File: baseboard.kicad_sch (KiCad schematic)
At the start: 27 parts, among them J10 AS7265X, J11 Conn_02x20_Odd_Even, J12 TFTLCD, J5 Screw_Terminal_01x02, J6 DCMI_CAMERA, J7 LCD_CHAR, J8 Conn_01x03, J9 Conn_01x03, U2 LM2676S-5, U3 AMS1117-3.3

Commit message: snapshot
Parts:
- removed J12: TFTLCD, Connector_PinHeader_2.54mm:PinHeader_1x09_P2.54mm_Vertical, symbol Connector_Generic:Conn_01x09
- added H1, H2, H3, H4: MountingHole, MountingHole:MountingHole_3.2mm_M3, symbol Mechanical:MountingHole
- added J13: UserGPIO, Connector_PinHeader_2.54mm:PinHeader_2x05_P2.54mm_Vertical, symbol Connector_Generic:Conn_02x05_Odd_Even
- added J14: TFT_LCD, Connector_PinHeader_2.54mm:PinHeader_1x14_P2.54mm_Vertical, symbol Connector_Generic:Conn_01x14
- J11: value Conn_02x20_Odd_Even -> TFT_LCD2
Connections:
- net GND: now also J13.1 (Pin_1), J13.10 (Pin_10), J13.3 (Pin_3), J13.5 (Pin_5), J13.7 (Pin_7), J13.9 (Pin_9), J14.2 (Pin_2)
- net PB0: now also J11.39 (Pin_39), J14.8 (Pin_8)
- net PB1: now also J14.5 (Pin_5)
- net PB12: now also J14.3 (Pin_3)
- net PB13: now also J14.7 (Pin_7)
- net PB14: now also J14.9 (Pin_9)
- net PB15: now also J14.6 (Pin_6)
- net PB8: now also J11.34 (Pin_34)
- net PB9: now also J11.35 (Pin_35)
- net PC4: now also J14.4 (Pin_4)
- net VCC: now also J14.1 (Pin_1)
- net PC5: now reaches J11.36 (Pin_36)
- net PC5: now also J14.14 (Pin_14)
- net TE renamed PD2
- new net PA0: J13.8 (Pin_8)
- new net PA15: J14.11 (Pin_11)
- new net PA5: J14.10 (Pin_10)
- new net PB4: J14.13 (Pin_13)
- new net PB5: J14.12 (Pin_12)
- new net PC0: J13.2 (Pin_2)
- new net PC2: J13.4 (Pin_4)
- new net PC3: J13.6 (Pin_6)
- no-connect marks 0 -> 14
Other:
- moved on the sheet: C11, C12, C13, C14, C15, C16, C17, D2, D3, D4, J11, J5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

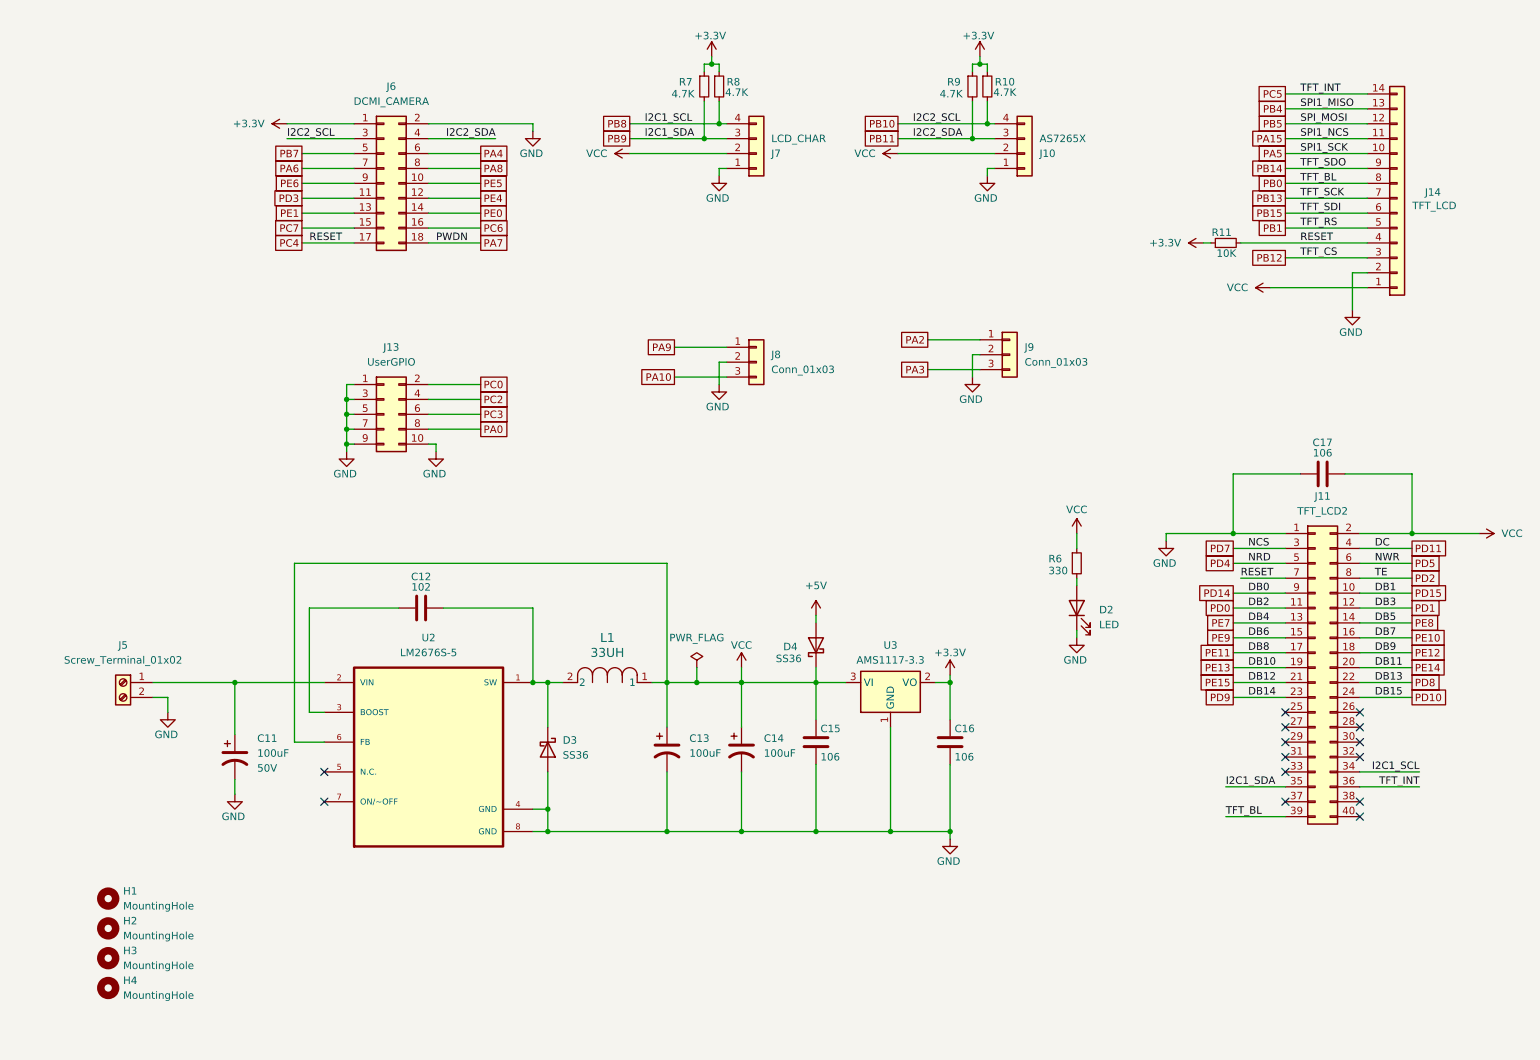
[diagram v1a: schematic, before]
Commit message: add servos and fan outputs
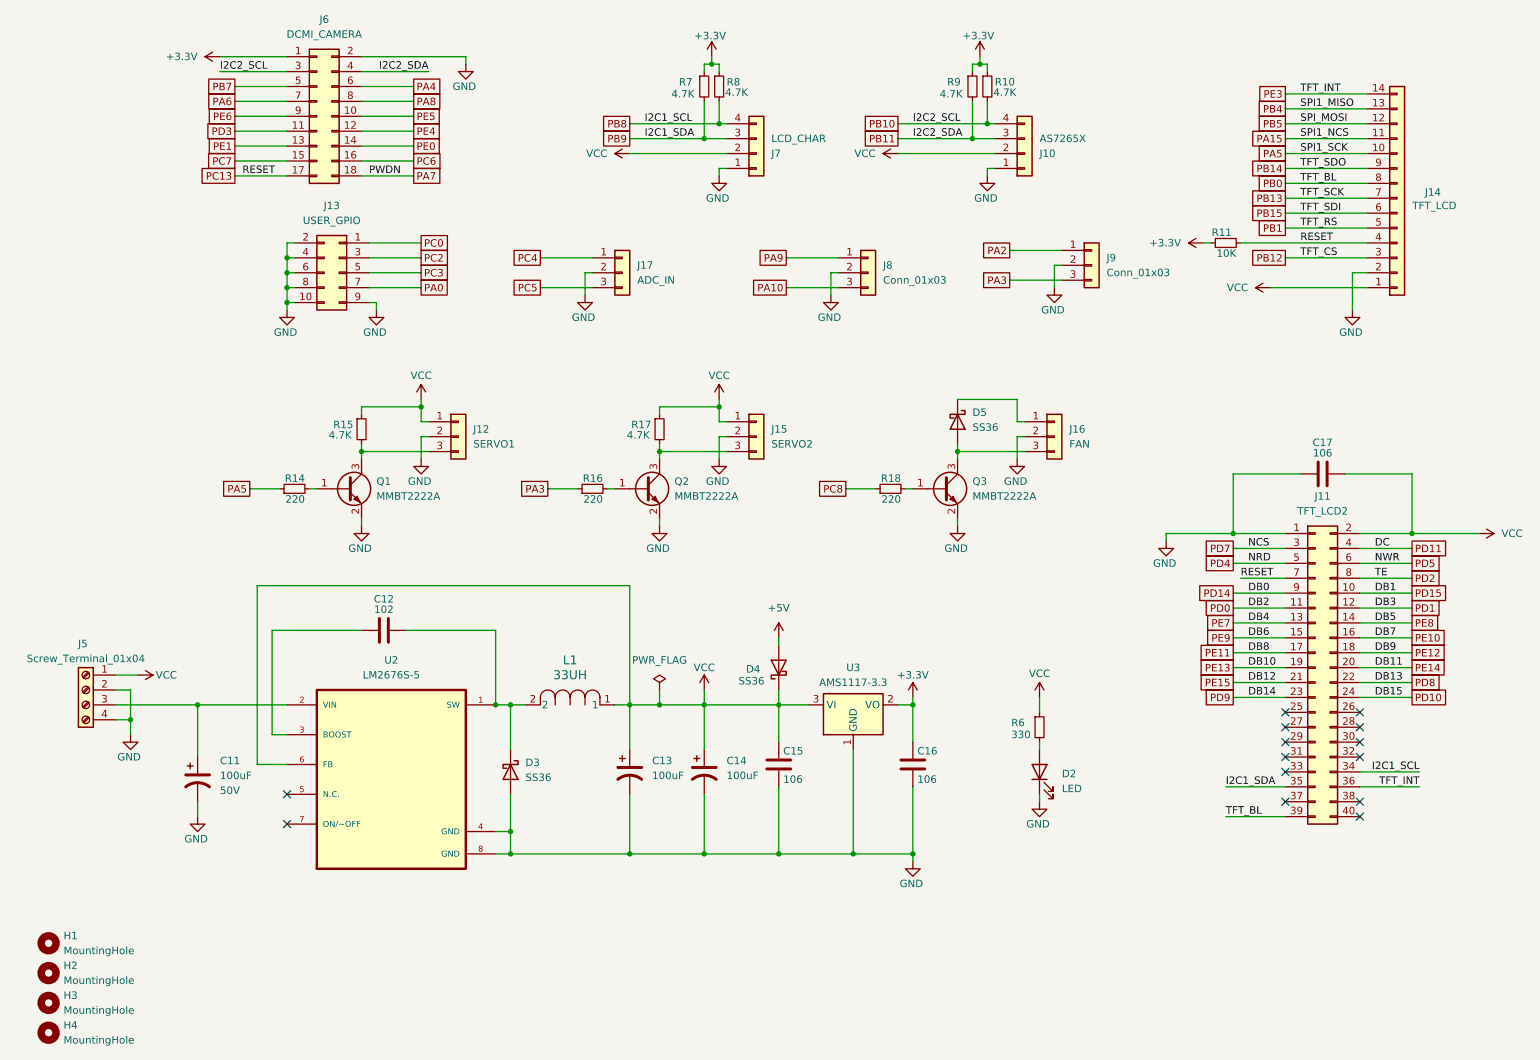
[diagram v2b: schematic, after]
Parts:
- removed J5: Screw_Terminal_01x02, TerminalBlock:TerminalBlock_MaiXu_MX126-5.0-02P_1x02_P5.00mm, symbol Connector:Screw_Terminal_01x02
- added D5: SS36, Diode_SMD:D_SMA, symbol LM2676S-3.3_NOPB:SS36
- added J12: SERVO1, Connector_PinHeader_2.54mm:PinHeader_1x03_P2.54mm_Vertical, symbol LM2676S-3.3_NOPB:Conn_01x03
- added J15: SERVO2, Connector_PinHeader_2.54mm:PinHeader_1x03_P2.54mm_Vertical, symbol LM2676S-3.3_NOPB:Conn_01x03
- added J16: FAN, Connector_PinHeader_2.54mm:PinHeader_1x03_P2.54mm_Vertical, symbol LM2676S-3.3_NOPB:Conn_01x03
- added J17: ADC_IN, Connector_PinHeader_2.54mm:PinHeader_1x03_P2.54mm_Vertical, symbol LM2676S-3.3_NOPB:Conn_01x03
- added J5: Screw_Terminal_01x04, TerminalBlock:TerminalBlock_MaiXu_MX126-5.0-04P_1x04_P5.00mm, symbol Connector:Screw_Terminal_01x04
- added Q1, Q2, Q3: MMBT2222A, Package_TO_SOT_SMD:SOT-23, symbol Transistor_BJT:MMBT2222A
- added R14, R16, R18: 220, Resistor_SMD:R_0805_2012Metric_Pad1.20x1.40mm_HandSolder, symbol LM2676S-3.3_NOPB:R_Small
- added R15, R17: 4.7K, Resistor_SMD:R_0805_2012Metric_Pad1.20x1.40mm_HandSolder, symbol LM2676S-3.3_NOPB:R_Small
- C11: symbol SparkFun-Capacitor:C_Polarized -> LM2676S-3.3_NOPB:C_Polarized
- C12: footprint Capacitor_THT:C_Disc_D7.5mm_W2.5mm_P5.00mm -> Capacitor_SMD:C_0603_1608Metric_Pad1.08x0.95mm_HandSolder; symbol Device:C -> LM2676S-3.3_NOPB:C
- C13, C14: symbol Device:C_Polarized_US -> LM2676S-3.3_NOPB:C_Polarized_US
- C15, C16, C17: footprint Capacitor_THT:C_Disc_D7.5mm_W2.5mm_P5.00mm -> Capacitor_SMD:C_0805_2012Metric_Pad1.18x1.45mm_HandSolder; symbol Device:C -> LM2676S-3.3_NOPB:C
- D2: symbol Device:LED -> LM2676S-3.3_NOPB:LED
- D3, D4: symbol Diode:SS36 -> LM2676S-3.3_NOPB:SS36
- H1, H2, H3, H4: symbol Mechanical:MountingHole -> LM2676S-3.3_NOPB:MountingHole
- J10, J7: symbol Connector_Generic:Conn_01x04 -> LM2676S-3.3_NOPB:Conn_01x04
- J11: symbol Connector_Generic:Conn_02x20_Odd_Even -> LM2676S-3.3_NOPB:Conn_02x20_Odd_Even
- J13: value UserGPIO -> USER_GPIO
- J14: symbol Connector_Generic:Conn_01x14 -> LM2676S-3.3_NOPB:Conn_01x14
- J6: symbol Connector_Generic:Conn_02x09_Odd_Even -> LM2676S-3.3_NOPB:Conn_02x09_Odd_Even
- J8, J9: symbol Connector_Generic:Conn_01x03 -> LM2676S-3.3_NOPB:Conn_01x03
- L1: symbol ul_CDRH104RNP:CDRH104RNP-330NC -> LM2676S-3.3_NOPB:CDRH104RNP-330NC
- R10, R11, R6, R7, R8, R9: footprint Resistor_THT:R_Axial_DIN0207_L6.3mm_D2.5mm_P10.16mm_Horizontal -> Resistor_SMD:R_0805_2012Metric_Pad1.20x1.40mm_HandSolder; symbol Device:R_Small -> LM2676S-3.3_NOPB:R_Small
- U3: symbol Regulator_Linear:AMS1117-3.3 -> LM2676S-3.3_NOPB:AMS1117-3.3
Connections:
- net GND: now also J13.2 (Pin_2), J13.4 (Pin_4), J13.6 (Pin_6), J13.8 (Pin_8), J12.2 (Pin_2), J15.2 (Pin_2), J16.2 (Pin_2), J17.2 (Pin_2), J5.2 (Pin_2), J5.4 (Pin_4), Q1.2 (E), Q2.2 (E), Q3.2 (E); no longer J13.1 (Pin_1), J13.3 (Pin_3), J13.5 (Pin_5), J13.7 (Pin_7)
- net PA0: now also J13.7 (Pin_7); no longer J13.8 (Pin_8)
- net PA3: now also R16.1
- net PA5: now also R14.1
- net PC0: now also J13.1 (Pin_1); no longer J13.2 (Pin_2)
- net PC2: now also J13.3 (Pin_3); no longer J13.4 (Pin_4)
- net PC3: now also J13.5 (Pin_5); no longer J13.6 (Pin_6)
- net PC4: now also J17.1 (Pin_1); no longer J11.7 (Pin_7), J14.4 (Pin_4), J6.17 (Pin_17), R11.2
- net PC5: now also J17.3 (Pin_3); no longer J11.36 (Pin_36), J14.14 (Pin_14)
- net VCC: now also J12.1 (Pin_1), J15.1 (Pin_1), J5.1 (Pin_1), R15.1, R17.1
- net at C11.1, U2.2 (VIN): now also J5.3 (Pin_3)
- new net: J15.3 (Pin_3), Q2.3 (C), R17.2
- new net: Q1.1 (B), R14.2
- new net: J12.3 (Pin_3), Q1.3 (C), R15.2
- new net: D5.1 (K), J16.1 (Pin_1)
- new net: D5.2 (A), J16.3 (Pin_3), Q3.3 (C)
- new net: Q2.1 (B), R16.2
- new net: Q3.1 (B), R18.2
- new net PC13: J11.7 (Pin_7), J14.4 (Pin_4), J6.17 (Pin_17), R11.2
- new net PC8: R18.1
- new net PE3: J11.36 (Pin_36), J14.14 (Pin_14)
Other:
- moved on the sheet: C11, C12, C13, C14, C15, C16, D2, D3, D4, H1, H2, H3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

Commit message: move servo connector closer to power supply
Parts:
- J8: value Conn_01x03 -> UART1
- J9: value Conn_01x03 -> UART2
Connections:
- net PA3: no longer J9.3 (Pin_3)
- new net PD6: J9.3 (Pin_3)
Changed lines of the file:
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@@
 		)
 	)
-	(global_label "PA3"
+	(global_label "PD6"
 		(shape passive)
 		(at 182.88 63.5 180)
@@
 		)
 		(property "Intersheetrefs" "${INTERSHEET_REFS}"
-			(at 177.438 63.5 0)
+			(at 177.2566 63.5 0)
 			(effects
 				(font
@@
 			)
 		)
-		(property "Value" "Conn_01x03"
+		(property "Value" "UART2"
 			(at 199.39 62.2299 0)
 			(effects
@@
 			)
 		)
-		(property "Value" "Conn_01x03"
+		(property "Value" "UART1"
 			(at 161.29 63.4999 0)
 			(effects

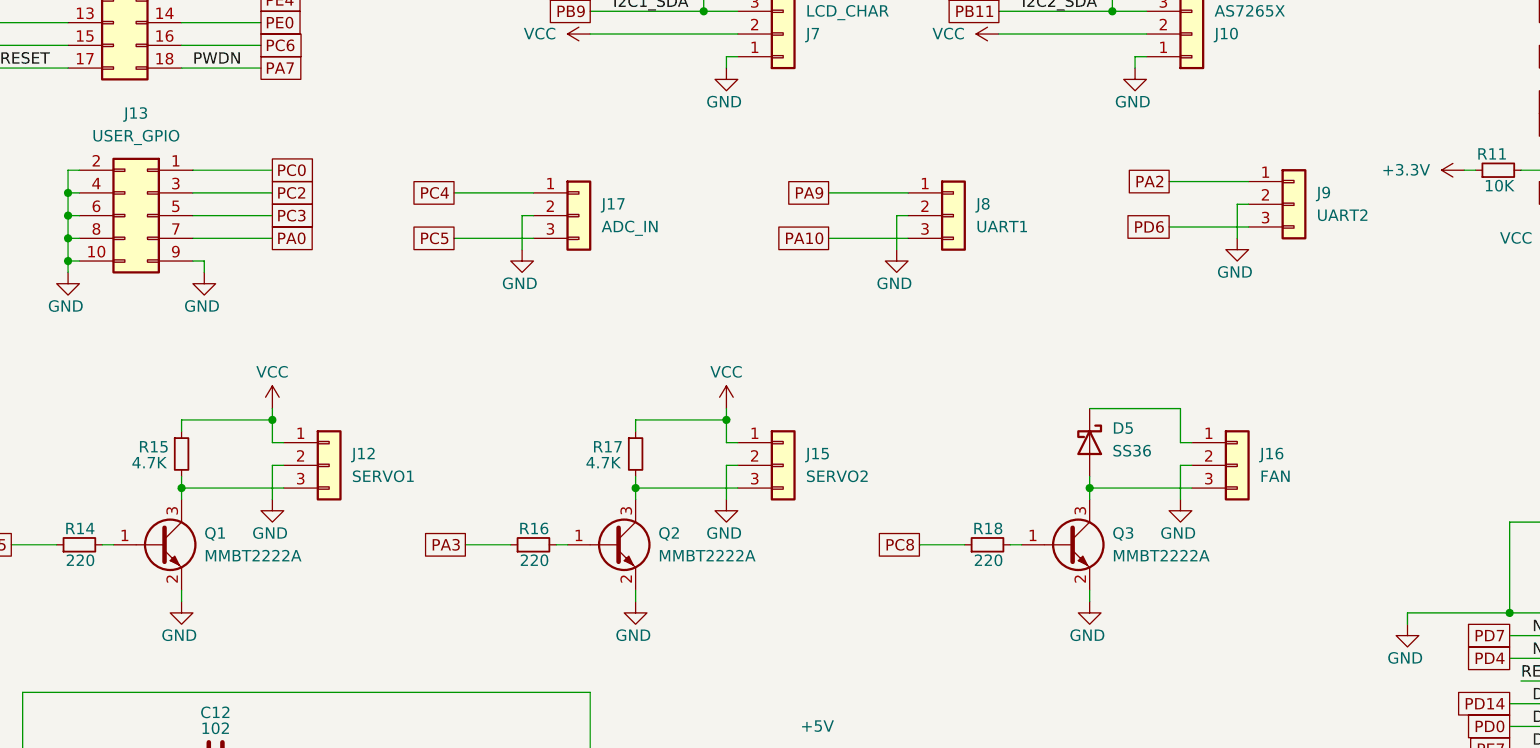
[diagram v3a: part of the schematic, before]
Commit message: change transistors from MMBT2222A to BCP56
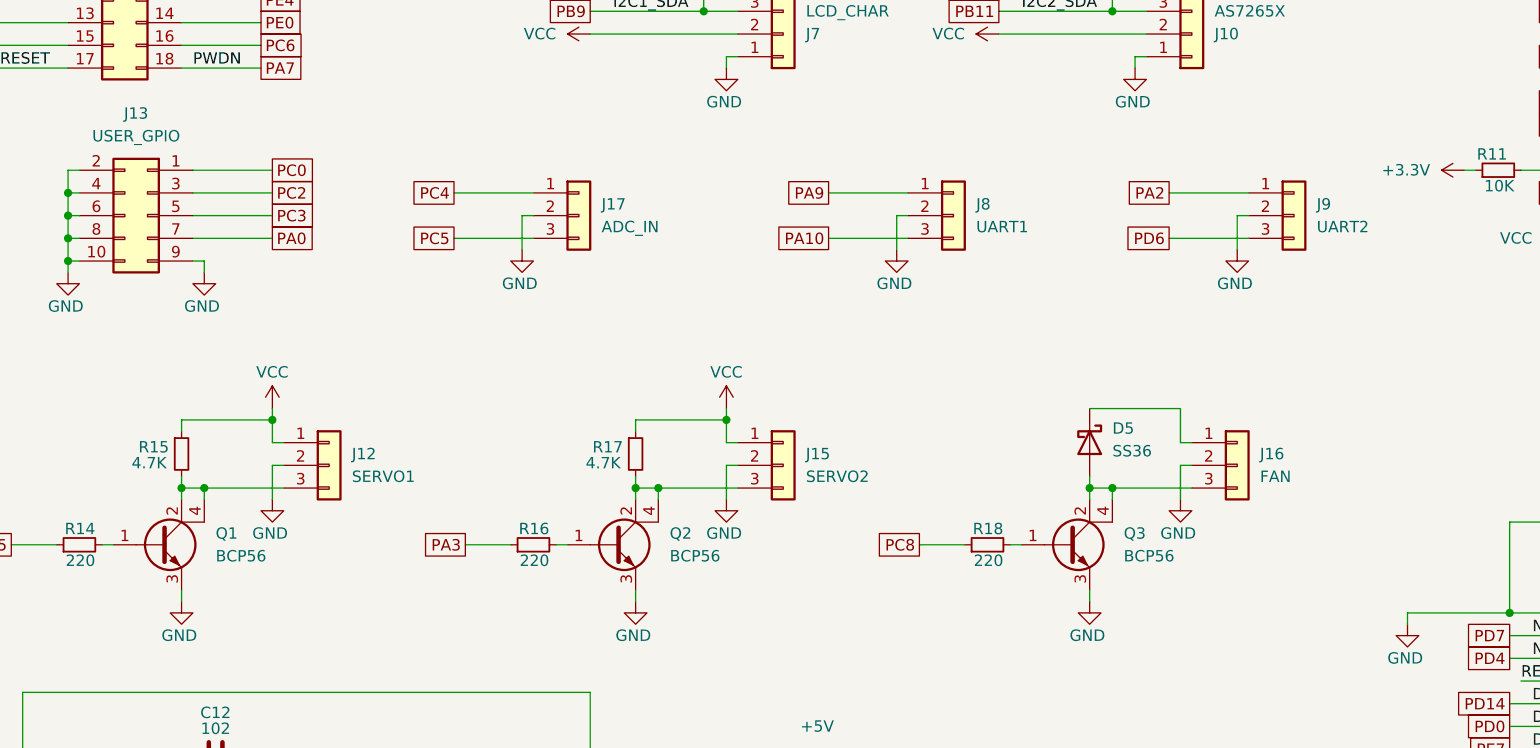
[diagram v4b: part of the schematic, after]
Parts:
- removed Q1, Q2, Q3: MMBT2222A, Package_TO_SOT_SMD:SOT-23, symbol Transistor_BJT:MMBT2222A
- added Q1, Q2, Q3: BCP56, Package_TO_SOT_SMD:SOT-223-3_TabPin2, symbol Transistor_BJT:BCP56
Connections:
- net GND: now also Q1.3 (E), Q2.3 (E), Q3.3 (E)
- net at J15.3 (Pin_3), R17.2: now also Q2.2 (C), Q2.4 (C)
- net at R14.2: now also Q1.1 (B)
- net at J12.3 (Pin_3), R15.2: now also Q1.2 (C), Q1.4 (C)
- net at D5.2 (A), J16.3 (Pin_3): now also Q3.2 (C), Q3.4 (C)
- net at R16.2: now also Q2.1 (B)
- net at R18.2: now also Q3.1 (B)
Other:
- moved on the sheet: J9
